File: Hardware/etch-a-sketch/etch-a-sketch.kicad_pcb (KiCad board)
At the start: 4 copper layers, 100 x 62 mm, 37 parts, among them J1 USART, J2 Conn_02x05_Odd_Even, J3 OLED, J4 Power Connector, SW1 Encoder 1, SW2 Encoder 2, U1 AMS1117-3.3, U2 STM32F401RET6

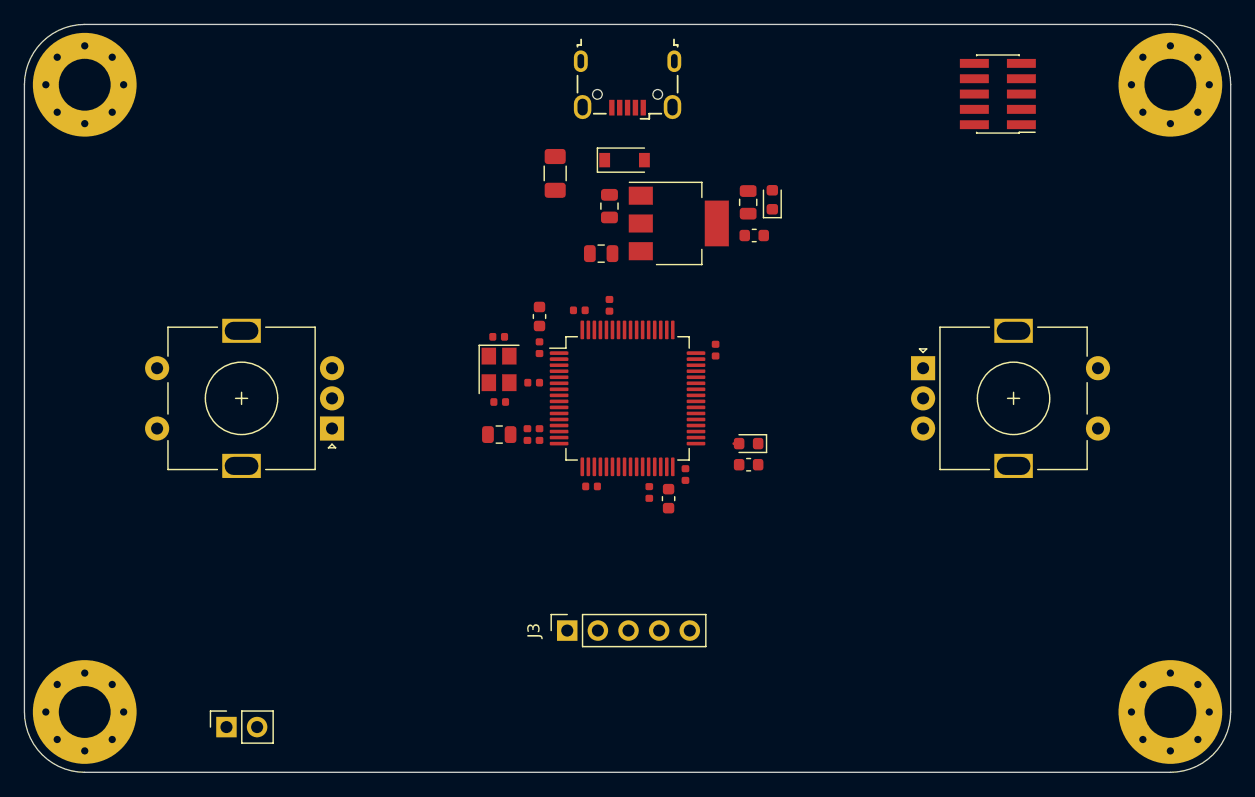
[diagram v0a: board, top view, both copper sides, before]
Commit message: feat: add GND and 3v3 fills to all layers
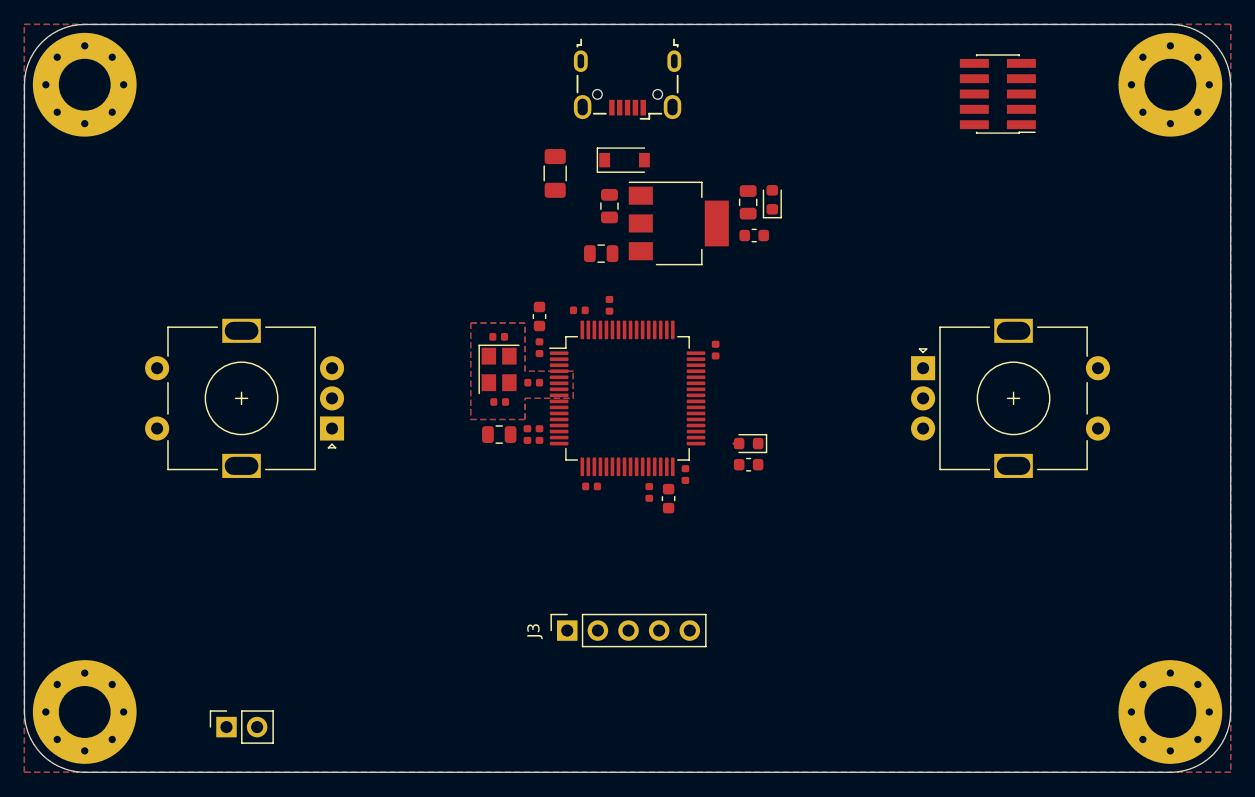
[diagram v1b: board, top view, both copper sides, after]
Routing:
- added copper zone on In2.Cu, net +3V3
- added copper zone on B.Cu, net GND
- added copper zone on F.Cu, net GND
- added copper zone on In1.Cu, net GND
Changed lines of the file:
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@@
   (layers
     (0 F.Cu signal)
-    (1 GND power)
-    (2 3V3 power)
+    (1 In1.Cu power)
+    (2 In2.Cu power)
     (31 B.Cu signal)
     (33 F.Adhes user)
@@
   (gr_line (start 120 25) (end 120 77) (layer Edge.Cuts) (width 0.05))
   (segment (start 79.25 54.75) (end 78.8125 54.75) (width 0.25) (layer F.Cu) (net 11))
+  (zone (net 1) (net_name GND) (layer In1.Cu) (hatch edge 0.508)
+    (connect_pads (clearance 0.508))
+    (min_thickness 0.254)
+    (fill yes (arc_segments 32) (thermal_gap 0.508) (thermal_bridge_width 0.508))
+    (polygon
+      (pts
+        (xy 120 20) (xy 120 82) (xy 20 82) (xy 20 20)
+      )
+    )
+    (polygon
+      (pts
+        (xy 61.5 51) (xy 65.5 51) (xy 65.5 48.75) (xy 61.5 48.75) (xy 61.5 44.75)
+        (xy 57 44.75) (xy 57 52.75) (xy 61.5 52.75)
+      )
+    )
+  )
+  (zone (net 3) (net_name +3V3) (layer In2.Cu) (hatch edge 0.508)
+    (connect_pads (clearance 0.508))
+    (min_thickness 0.254)
+    (fill yes (arc_segments 32) (thermal_gap 0.508) (thermal_bridge_width 0.508))
+    (polygon
+      (pts
+        (xy 120 20) (xy 120 82) (xy 20 82) (xy 20 20)
+      )
+    )
+    (polygon
+      (pts
+        (xy 61.5 51) (xy 65.5 51) (xy 65.5 48.75) (xy 61.5 48.75) (xy 61.5 44.75)
+        (xy 57 44.75) (xy 57 52.75) (xy 61.5 52.75)
+      )
+    )
+  )
+  (zone (net 1) (net_name GND) (layer F.Cu) (hatch edge 0.508)
+    (connect_pads (clearance 0.508))
+    (min_thickness 0.254)
+    (fill yes (arc_segments 32) (thermal_gap 0.508) (thermal_bridge_width 0.508))
+    (polygon
+      (pts
+        (xy 120 20) (xy 120 82) (xy 20 82) (xy 20 20)
+      )
+    )
+    (polygon
+      (pts
+        (xy 61.5 51) (xy 65.5 51) (xy 65.5 48.75) (xy 61.5 48.75) (xy 61.5 44.75)
+        (xy 57 44.75) (xy 57 52.75) (xy 61.5 52.75)
+      )
+    )
+  )
+  (zone (net 1) (net_name GND) (layer B.Cu) (hatch edge 0.508)
+    (connect_pads (clearance 0.508))
+    (min_thickness 0.254)
+    (fill yes (arc_segments 32) (thermal_gap 0.508) (thermal_bridge_width 0.508))
+    (polygon
+      (pts
+        (xy 120 20) (xy 120 82) (xy 20 82) (xy 20 20)
+      )
+    )
+    (polygon
+      (pts
+        (xy 61.5 51) (xy 65.5 51) (xy 65.5 48.75) (xy 61.5 48.75) (xy 61.5 44.75)
+        (xy 57 44.75) (xy 57 52.75) (xy 61.5 52.75)
+      )
+    )
+  )
 )

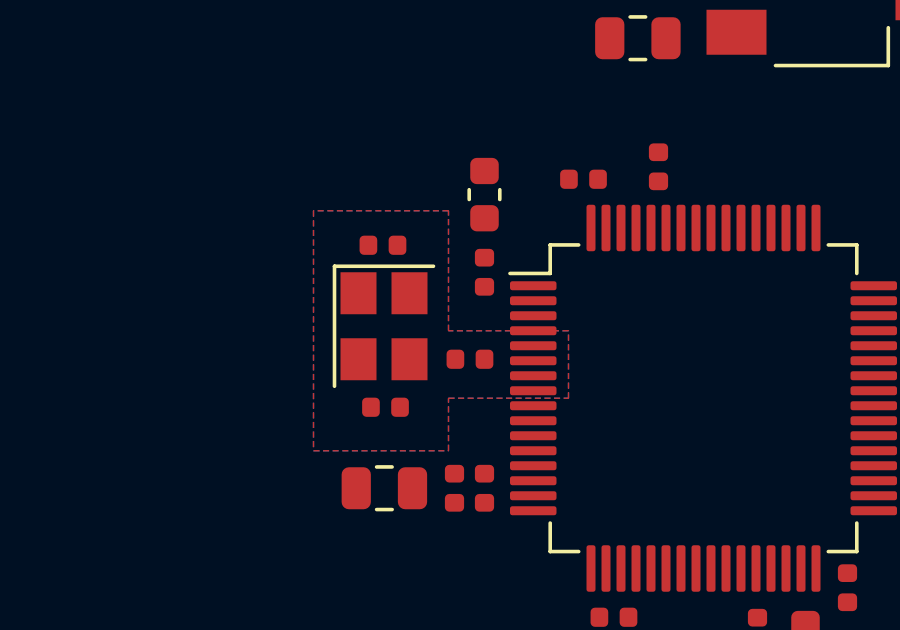
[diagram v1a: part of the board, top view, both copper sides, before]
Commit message: feat: route oscillator and refine fills
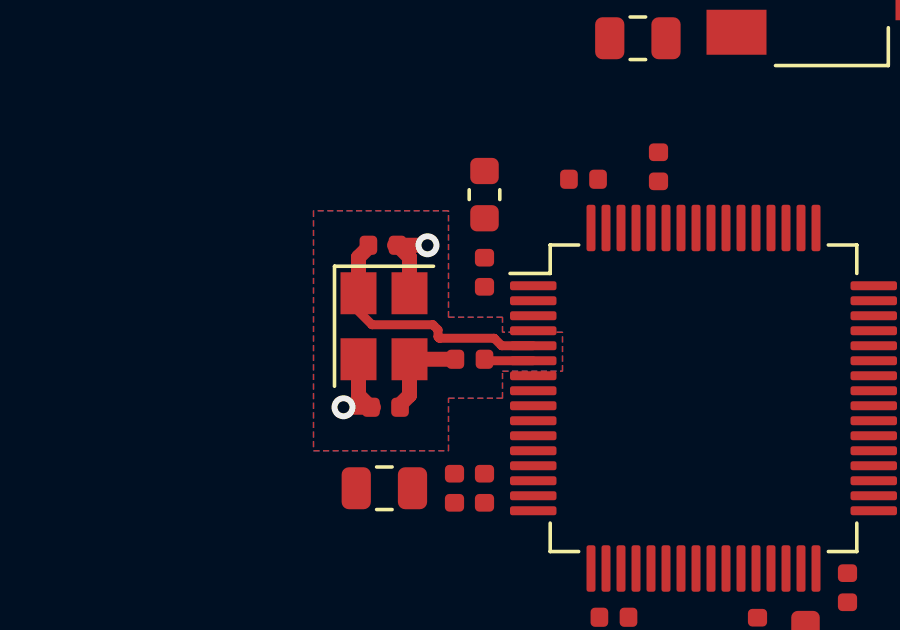
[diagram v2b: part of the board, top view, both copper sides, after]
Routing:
- net HSE_IN: track 0.00 -> 8.06 mm
- net GND: track 0.00 -> 5.35 mm, vias 0 -> 2
- net Net-(C13-Pad1): track 0.00 -> 3.12 mm
- net HSE_OUT: track 0.00 -> 1.48 mm
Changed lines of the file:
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@@
     (thickness 1.6)
     (drawings 8)
-    (tracks 1)
+    (tracks 23)
     (zones 0)
     (modules 37)
@@
   )
   (setup
-    (last_trace_width 0.25)
+    (last_trace_width 0.3)
     (user_trace_width 0.3)
     (user_trace_width 0.4)
@@
   (gr_line (start 115 82) (end 25 82) (layer Edge.Cuts) (width 0.05))
   (gr_line (start 120 25) (end 120 77) (layer Edge.Cuts) (width 0.05))
+  (via (at 60.8 45.9) (size 0.8) (drill 0.4) (layers F.Cu B.Cu) (net 1))
+  (via (at 58 51.3) (size 0.8) (drill 0.4) (layers F.Cu B.Cu) (net 1))
+  (segment (start 58 51.3) (end 59 51.3) (width 0.5) (layer F.Cu) (net 1))
+  (segment (start 60.8 45.9) (end 59.7 45.9) (width 0.5) (layer F.Cu) (net 1))
+  (segment (start 60.2 46.3) (end 59.9 46) (width 0.5) (layer F.Cu) (net 1))
+  (segment (start 60.2 47.5) (end 60.2 46.3) (width 0.5) (layer F.Cu) (net 1))
+  (segment (start 58.5 50.9) (end 58.8 51.2) (width 0.5) (layer F.Cu) (net 1))
+  (segment (start 58.5 49.7) (end 58.5 50.9) (width 0.5) (layer F.Cu) (net 1))
+  (segment (start 58.5 46.3) (end 58.8 46) (width 0.5) (layer F.Cu) (net 6))
+  (segment (start 58.5 47.5) (end 58.5 46.3) (width 0.5) (layer F.Cu) (net 6))
+  (segment (start 63.273586 49.25) (end 63.023586 49) (width 0.3) (layer F.Cu) (net 6))
+  (segment (start 64.325 49.25) (end 63.273586 49.25) (width 0.3) (layer F.Cu) (net 6))
+  (segment (start 61.150001 48.950001) (end 61.150001 48.719999) (width 0.3) (layer F.Cu) (net 6))
+  (segment (start 61.2 49) (end 61.150001 48.950001) (width 0.3) (layer F.Cu) (net 6))
+  (segment (start 63.023586 49) (end 61.2 49) (width 0.3) (layer F.Cu) (net 6))
+  (segment (start 60.980003 48.550001) (end 58.950001 48.550001) (width 0.3) (layer F.Cu) (net 6))
+  (segment (start 61.150001 48.719999) (end 60.980003 48.550001) (width 0.3) (layer F.Cu) (net 6))
+  (segment (start 58.950001 48.550001) (end 58.5 48.1) (width 0.3) (layer F.Cu) (net 6))
+  (segment (start 60.2 50.9) (end 59.9 51.2) (width 0.5) (layer F.Cu) (net 7))
+  (segment (start 60.2 49.7) (end 60.2 50.9) (width 0.5) (layer F.Cu) (net 7))
+  (segment (start 60.2 49.7) (end 61.7 49.7) (width 0.5) (layer F.Cu) (net 7))
   (segment (start 79.25 54.75) (end 78.8125 54.75) (width 0.25) (layer F.Cu) (net 11))
+  (segment (start 64.325 49.75) (end 62.85 49.75) (width 0.3) (layer F.Cu) (net 29))
+  (zone (net 1) (net_name GND) (layer F.Cu) (hatch edge 0.508)
+    (connect_pads (clearance 0.508))
+    (min_thickness 0.254)
+    (fill yes (arc_segments 32) (thermal_gap 0.508) (thermal_bridge_width 0.508))
+    (polygon
+      (pts
+        (xy 120 20) (xy 120 82) (xy 20 82) (xy 20 20)
+      )
+    )
+    (polygon
+      (pts
+        (xy 61.5 51) (xy 63.3 51) (xy 63.3 50.1) (xy 65.3 50.1) (xy 65.3 48.8)
+        (xy 63.3 48.8) (xy 63.3 48.3) (xy 61.5 48.3) (xy 61.5 44.75) (xy 57 44.75)
+        (xy 57 52.75) (xy 61.5 52.75)
+      )
+    )
+  )
+  (zone (net 1) (net_name GND) (layer In1.Cu) (hatch edge 0.508)
+    (connect_pads (clearance 0.508))
+    (min_thickness 0.254)
+    (fill yes (arc_segments 32) (thermal_gap 0.508) (thermal_bridge_width 0.508))
+    (polygon
+      (pts
+        (xy 61.4 48.7) (xy 61.6 48.7) (xy 63.1 48.7) (xy 63.5 49.1) (xy 65.2 49.1)
+        (xy 65.2 50) (xy 63.2 50) (xy 63.2 50.35) (xy 61.427296 50.35) (xy 61.427296 52.1)
+        (xy 57.677296 52.1) (xy 57.677296 45.35) (xy 61.4 45.35)
+      )
+    )
+  )
   (zone (net 1) (net_name GND) (layer In1.Cu) (hatch edge 0.508)
     (connect_pads (clearance 0.508))
@@
     (polygon
       (pts
-        (xy 61.5 51) (xy 65.5 51) (xy 65.5 48.75) (xy 61.5 48.75) (xy 61.5 44.75)
-        (xy 57 44.75) (xy 57 52.75) (xy 61.5 52.75)
+        (xy 61.5 51) (xy 63.3 51) (xy 63.3 50.1) (xy 65.3 50.1) (xy 65.3 48.8)
+        (xy 63.3 48.8) (xy 63.3 48.3) (xy 61.5 48.3) (xy 61.5 44.75) (xy 57 44.75)
+        (xy 57 52.75) (xy 61.5 52.75)
       )
     )
@@
     (polygon
       (pts
-        (xy 61.5 51) (xy 65.5 51) (xy 65.5 48.75) (xy 61.5 48.75) (xy 61.5 44.75)
-        (xy 57 44.75) (xy 57 52.75) (xy 61.5 52.75)
-      )
-    )
-  )
-  (zone (net 1) (net_name GND) (layer F.Cu) (hatch edge 0.508)
-    (connect_pads (clearance 0.508))
-    (min_thickness 0.254)
-    (fill yes (arc_segments 32) (thermal_gap 0.508) (thermal_bridge_width 0.508))
-    (polygon
-      (pts
-        (xy 120 20) (xy 120 82) (xy 20 82) (xy 20 20)
-      )
-    )
-    (polygon
-      (pts
-        (xy 61.5 51) (xy 65.5 51) (xy 65.5 48.75) (xy 61.5 48.75) (xy 61.5 44.75)
-        (xy 57 44.75) (xy 57 52.75) (xy 61.5 52.75)
+        (xy 61.5 51) (xy 63.3 51) (xy 63.3 50.1) (xy 65.3 50.1) (xy 65.3 48.8)
+        (xy 63.3 48.8) (xy 63.3 48.3) (xy 61.5 48.3) (xy 61.5 44.75) (xy 57 44.75)
+        (xy 57 52.75) (xy 61.5 52.75)
       )
     )
@@
     (polygon
       (pts
-        (xy 61.5 51) (xy 65.5 51) (xy 65.5 48.75) (xy 61.5 48.75) (xy 61.5 44.75)
-        (xy 57 44.75) (xy 57 52.75) (xy 61.5 52.75)
+        (xy 61.5 51) (xy 63.3 51) (xy 63.3 50.1) (xy 65.3 50.1) (xy 65.3 48.8)
+        (xy 63.3 48.8) (xy 63.3 48.3) (xy 61.5 48.3) (xy 61.5 44.75) (xy 57 44.75)
+        (xy 57 52.75) (xy 61.5 52.75)
       )
     )

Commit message: feat: add small trace between osc fill and In1.Cu full
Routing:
- net GND: track 5.35 -> 7.05 mm
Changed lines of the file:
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@@
     (thickness 1.6)
     (drawings 8)
-    (tracks 23)
+    (tracks 24)
     (zones 0)
     (modules 37)
@@
   )
   (setup
-    (last_trace_width 0.3)
+    (last_trace_width 0.5)
     (user_trace_width 0.3)
     (user_trace_width 0.4)
@@
   (segment (start 58.5 50.9) (end 58.8 51.2) (width 0.5) (layer F.Cu) (net 1))
   (segment (start 58.5 49.7) (end 58.5 50.9) (width 0.5) (layer F.Cu) (net 1))
+  (segment (start 58 51.3) (end 58 53) (width 0.5) (layer In1.Cu) (net 1))
   (segment (start 58.5 46.3) (end 58.8 46) (width 0.5) (layer F.Cu) (net 6))
   (segment (start 58.5 47.5) (end 58.5 46.3) (width 0.5) (layer F.Cu) (net 6))

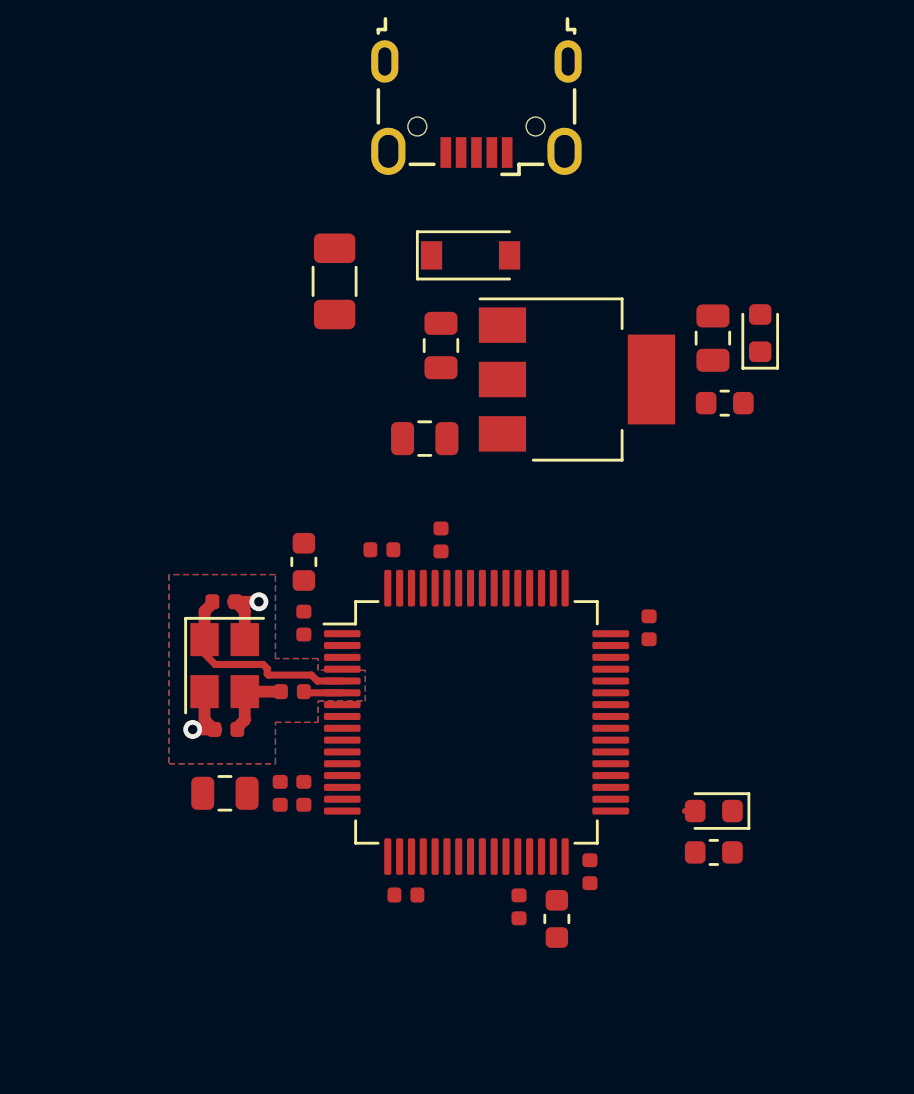
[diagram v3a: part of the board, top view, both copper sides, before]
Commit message: feat: route power
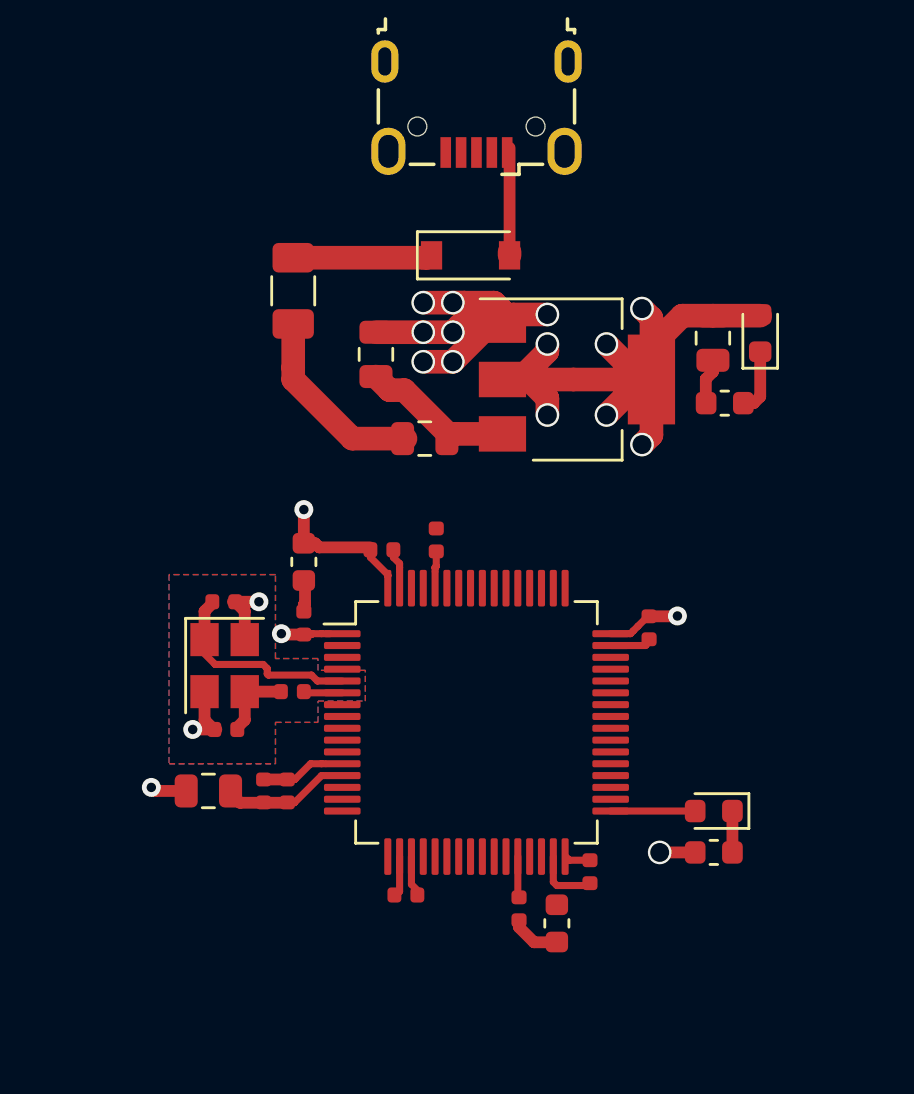
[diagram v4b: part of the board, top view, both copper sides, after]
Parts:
- moved C1 2.78 mm to (65.8, 35.4)
- moved F1 1.80 mm to (62.2, 32.8)
- moved C10 0.71 mm to (61.0, 53.9)
- moved C9 0.71 mm to (62.0, 53.9)
- moved FB2 0.71 mm to (58.7, 53.9)
- moved R2 0.20 mm to (68.3, 43.3)
- moved C11 0.19 mm to (73.4, 59.5)
- moved R3 0.09 mm to (71.8, 58.9)
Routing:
- net +3V3: track 0.00 -> 46.5 mm, vias 0 -> 10
- net GND: track 7.05 -> 40.1 mm, vias 2 -> 10
- net Net-(F1-Pad2): track 0.00 -> 8.14 mm
- net Net-(C1-Pad1): track 0.00 -> 6.47 mm
- net Net-(D1-Pad1): track 0.00 -> 5.79 mm
- net +3.3VA: track 0.00 -> 4.85 mm
- net VCC: track 0.00 -> 4.70 mm
- net Net-(D3-Pad2): track 0.44 -> 4.08 mm
- net Net-(D2-Pad1): track 0.00 -> 2.75 mm
- net Net-(D3-Pad1): track 0.00 -> 1.76 mm
- net BOOT1: track 0.00 -> 1.75 mm
- net BOOT0: track 0.00 -> 0.85 mm
